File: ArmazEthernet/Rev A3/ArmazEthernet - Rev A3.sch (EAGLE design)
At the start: 109 parts, among them J1 22-05-7028-02, P1 RB1-125BAG1A, T1 H1102FNL, T2 H1102FNL, U3 KSZ8995MA, U4 AT24C02C-SSHM-B, X1 NE8FAV, X2 NE8FAV, Y1 8Z-25.000MHZMAAJ-T

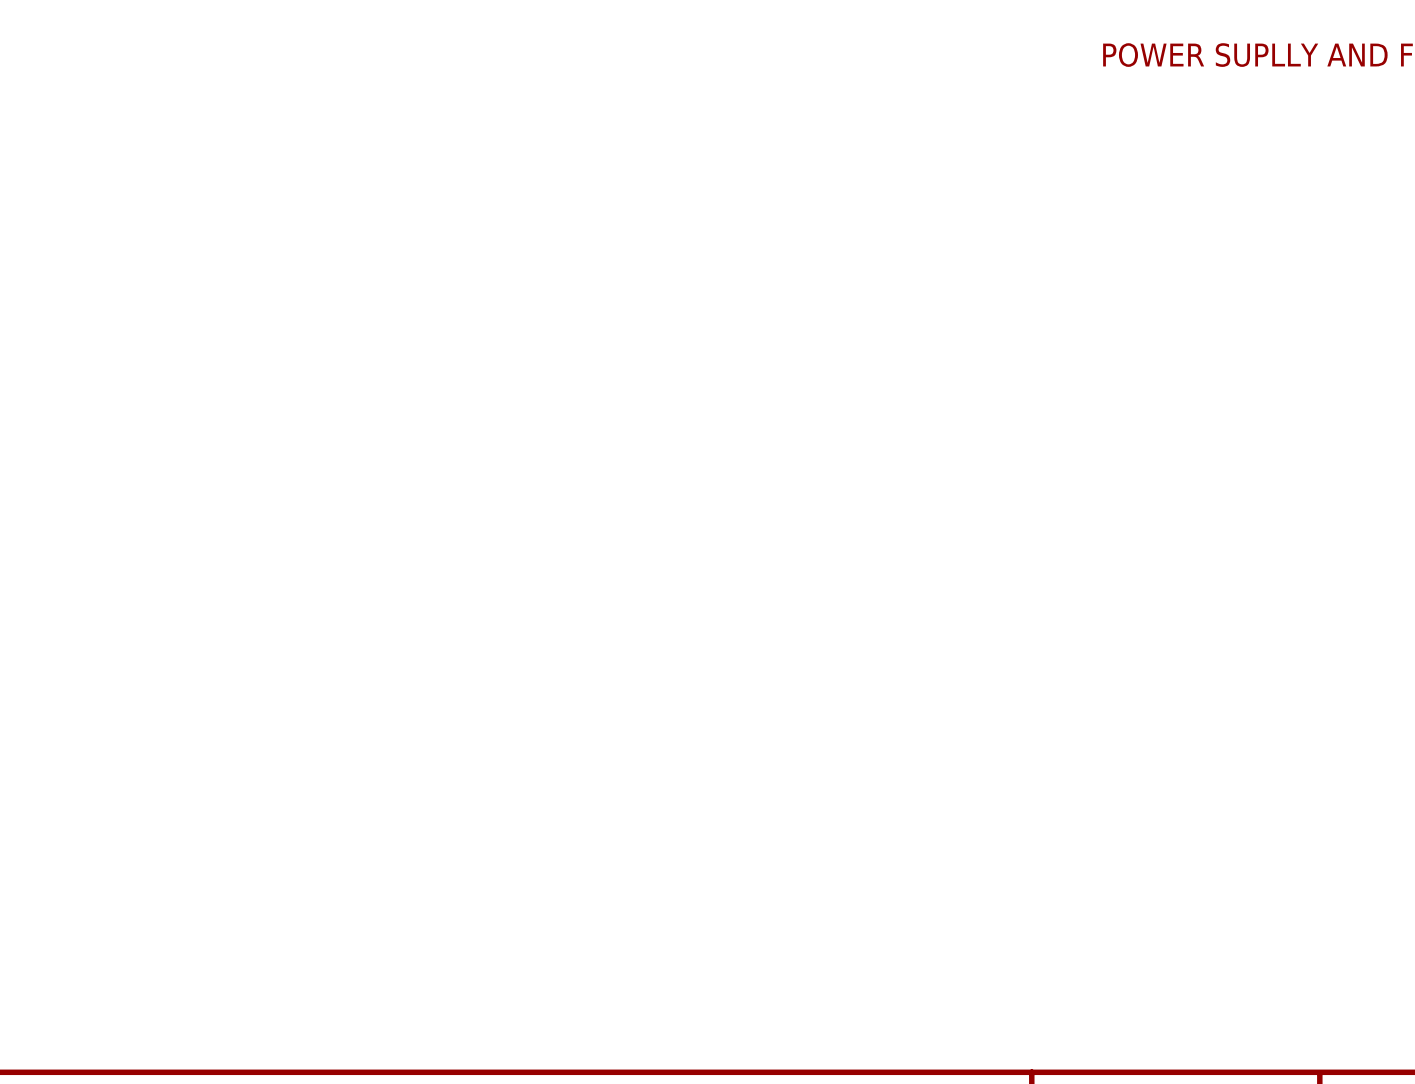
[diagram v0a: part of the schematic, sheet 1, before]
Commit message: Change the 3V3 and 1V8 circuit and place the component
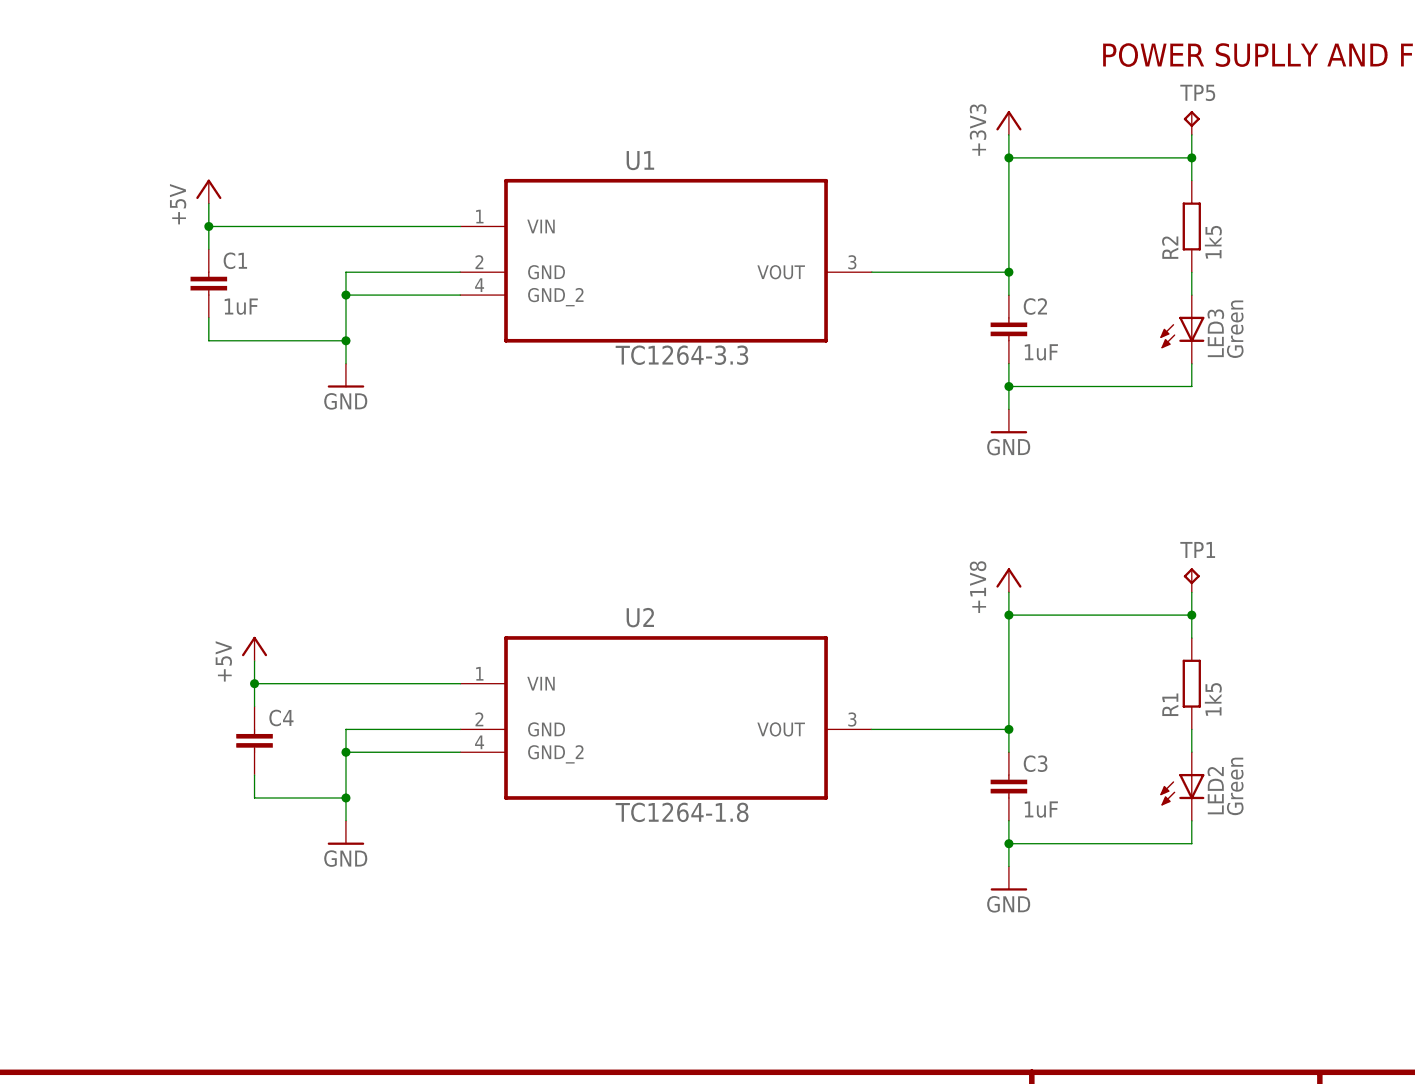
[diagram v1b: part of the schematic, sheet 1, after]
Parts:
- added C1, C2, C3: 1uF, rcl:C-EUC0603
- added C4: (no value), rcl:C-EUC0603
- added LED2, LED3: Green, led:LEDCHIP-LED0603
- added R1, R2: 1k5, rcl:R-EU_R0603
- added TP1, TP5: TPB1,27, testpad:TPB1,27
- added U1: TC1264-3.3, microchip-6:TC1264-3.3
- added U2: TC1264-1.8, microchip-6:TC1264-1.8
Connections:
- new net N$2: LED2.A, R1.1
- new net N$6: LED3.A, R2.1
- net +1V8: now also C3.1, R1.2, TP1.TP, U2.VOUT
- net +3V3: now also C2.1, R2.2, TP5.TP, U1.VOUT
- net +5V: now also C1.1, C4.1, U1.VIN, U2.VIN
- net GND: now also C1.2, C2.2, C3.2, C4.2, LED2.C, LED3.C, U1.GND, U1.GND_2, U2.GND, U2.GND_2

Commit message: switch the ethernet port on micrel component to improve the route : eth1 -> 3, eth2 -> 1 and eth 3-> 2
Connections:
- net L1-1: now also U3B.LED3-0; no longer U3B.LED1-0
- net L1-2: now also U3B.LED3-1; no longer U3B.LED1-1
- net L2-1: now also U3B.LED1-0; no longer U3B.LED2-0
- net L2-2: now also U3B.LED1-1; no longer U3B.LED2-1
- net L3-1: now also U3B.LED2-0; no longer U3B.LED3-0
- net L3-2: now also U3B.LED2-1; no longer U3B.LED3-1
- net RX1_ISO_N: now also U3A.RXM3; no longer U3A.RXM1
- net RX1_ISO_P: now also U3A.RXP3; no longer U3A.RXP1
- net RX2_ISO_N: now also U3A.RXM1; no longer U3A.RXM2
- net RX2_ISO_P: now also U3A.RXP1; no longer U3A.RXP2
- net RX3_ISO_N: now also U3A.RXM2; no longer U3A.RXM3
- net RX3_ISO_P: now also U3A.RXP2; no longer U3A.RXP3
- net TX1_ISO_N: now also U3A.TXM3; no longer U3A.TXM1
- net TX1_ISO_P: now also U3A.TXP3; no longer U3A.TXP1
- net TX2_ISO_N: now also U3A.TXM1; no longer U3A.TXM2
- net TX2_ISO_P: now also U3A.TXP1; no longer U3A.TXP2
- net TX3_ISO_N: now also U3A.TXM2; no longer U3A.TXM3
- net TX3_ISO_P: now also U3A.TXP2; no longer U3A.TXP3
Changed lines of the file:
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@@
 <net name="RX3_ISO_P" class="0">
 <segment>
-<wire x1="157.48" y1="205.74" x2="149.86" y2="205.74" width="0.1524" layer="91"/>
-<label x="149.86" y="205.74" size="1.27" layer="95" rot="R180" xref="yes"/>
-<pinref part="U3" gate="A" pin="RXP3"/>
+<wire x1="157.48" y1="220.98" x2="147.32" y2="220.98" width="0.1524" layer="91"/>
+<label x="147.32" y="220.98" size="1.27" layer="95" rot="R180" xref="yes"/>
+<pinref part="U3" gate="A" pin="RXP2"/>
 </segment>
 </net>
 <net name="RX3_ISO_N" class="0">
 <segment>
-<wire x1="157.48" y1="203.2" x2="149.86" y2="203.2" width="0.1524" layer="91"/>
-<label x="149.86" y="203.2" size="1.27" layer="95" rot="R180" xref="yes"/>
-<pinref part="U3" gate="A" pin="RXM3"/>
+<wire x1="157.48" y1="218.44" x2="147.32" y2="218.44" width="0.1524" layer="91"/>
+<label x="147.32" y="218.44" size="1.27" layer="95" rot="R180" xref="yes"/>
+<pinref part="U3" gate="A" pin="RXM2"/>
 </segment>
 </net>
 <net name="TX3_ISO_N" class="0">
 <segment>
-<wire x1="238.76" y1="172.72" x2="246.38" y2="172.72" width="0.1524" layer="91"/>
-<label x="246.38" y="172.72" size="1.27" layer="95" xref="yes"/>
-<pinref part="U3" gate="A" pin="TXM3"/>
+<wire x1="238.76" y1="165.1" x2="246.38" y2="165.1" width="0.1524" layer="91"/>
+<label x="246.38" y="165.1" size="1.27" layer="95" xref="yes"/>
+<pinref part="U3" gate="A" pin="TXM2"/>
 </segment>
 </net>
 <net name="TX3_ISO_P" class="0">
 <segment>
-<wire x1="238.76" y1="170.18" x2="246.38" y2="170.18" width="0.1524" layer="91"/>
-<label x="246.38" y="170.18" size="1.27" layer="95" xref="yes"/>
-<pinref part="U3" gate="A" pin="TXP3"/>
+<wire x1="238.76" y1="162.56" x2="246.38" y2="162.56" width="0.1524" layer="91"/>
+<label x="246.38" y="162.56" size="1.27" layer="95" xref="yes"/>
+<pinref part="U3" gate="A" pin="TXP2"/>
 </segment>
 </net>
@@
 <net name="L3-1" class="0">
 <segment>
-<pinref part="U3" gate="B" pin="LED3-0"/>
-<wire x1="241.3" y1="78.74" x2="251.46" y2="78.74" width="0.1524" layer="91"/>
-<label x="251.46" y="78.74" size="1.27" layer="95" xref="yes"/>
+<wire x1="241.3" y1="91.44" x2="251.46" y2="91.44" width="0.1524" layer="91"/>
+<label x="251.46" y="91.44" size="1.27" layer="95" xref="yes"/>
+<pinref part="U3" gate="B" pin="LED2-0"/>
 </segment>
 </net>
 <net name="L3-2" class="0">
 <segment>
-<pinref part="U3" gate="B" pin="LED3-1"/>
-<wire x1="241.3" y1="76.2" x2="251.46" y2="76.2" width="0.1524" layer="91"/>
-<label x="251.46" y="76.2" size="1.27" layer="95" xref="yes"/>
+<wire x1="241.3" y1="88.9" x2="251.46" y2="88.9" width="0.1524" layer="91"/>
+<label x="251.46" y="88.9" size="1.27" layer="95" xref="yes"/>
+<pinref part="U3" gate="B" pin="LED2-1"/>
 </segment>
 </net>
@@
 <net name="L1-1" class="0">
 <segment>
-<pinref part="U3" gate="B" pin="LED1-0"/>
+<wire x1="241.3" y1="78.74" x2="251.46" y2="78.74" width="0.1524" layer="91"/>
+<label x="251.46" y="78.74" size="1.27" layer="95" xref="yes"/>
+<pinref part="U3" gate="B" pin="LED3-0"/>
+</segment>
+</net>
+<net name="L1-2" class="0">
+<segment>
+<wire x1="241.3" y1="76.2" x2="251.46" y2="76.2" width="0.1524" layer="91"/>
+<label x="251.46" y="76.2" size="1.27" layer="95" xref="yes"/>
+<pinref part="U3" gate="B" pin="LED3-1"/>
+</segment>
+</net>
+<net name="L2-1" class="0">
+<segment>
 <wire x1="241.3" y1="99.06" x2="251.46" y2="99.06" width="0.1524" layer="91"/>
 <label x="251.46" y="99.06" size="1.27" layer="95" xref="yes"/>
-</segment>
-</net>
-<net name="L1-2" class="0">
-<segment>
-<pinref part="U3" gate="B" pin="LED1-1"/>
+<pinref part="U3" gate="B" pin="LED1-0"/>
+</segment>
+</net>
+<net name="L2-2" class="0">
+<segment>
 <wire x1="241.3" y1="96.52" x2="251.46" y2="96.52" width="0.1524" layer="91"/>
 <label x="251.46" y="96.52" size="1.27" layer="95" xref="yes"/>
-</segment>
-</net>
-<net name="L2-1" class="0">
-<segment>
-<pinref part="U3" gate="B" pin="LED2-0"/>
-<wire x1="241.3" y1="91.44" x2="251.46" y2="91.44" width="0.1524" layer="91"/>
-<label x="251.46" y="91.44" size="1.27" layer="95" xref="yes"/>
-</segment>
-</net>
-<net name="L2-2" class="0">
-<segment>
-<pinref part="U3" gate="B" pin="LED2-1"/>
-<wire x1="241.3" y1="88.9" x2="251.46" y2="88.9" width="0.1524" layer="91"/>
-<label x="251.46" y="88.9" size="1.27" layer="95" xref="yes"/>
+<pinref part="U3" gate="B" pin="LED1-1"/>
 </segment>
 </net>
 <net name="RX1_ISO_P" class="0">
 <segment>
+<wire x1="157.48" y1="205.74" x2="147.32" y2="205.74" width="0.1524" layer="91"/>
+<label x="147.32" y="205.74" size="1.27" layer="95" rot="R180" xref="yes"/>
+<pinref part="U3" gate="A" pin="RXP3"/>
+</segment>
+</net>
+<net name="RX1_ISO_N" class="0">
+<segment>
+<wire x1="157.48" y1="203.2" x2="147.32" y2="203.2" width="0.1524" layer="91"/>
+<label x="147.32" y="203.2" size="1.27" layer="95" rot="R180" xref="yes"/>
+<pinref part="U3" gate="A" pin="RXM3"/>
+</segment>
+</net>
+<net name="RX2_ISO_P" class="0">
+<segment>
+<wire x1="157.48" y1="231.14" x2="147.32" y2="231.14" width="0.1524" layer="91"/>
+<label x="147.32" y="231.14" size="1.27" layer="95" rot="R180" xref="yes"/>
 <pinref part="U3" gate="A" pin="RXP1"/>
-<wire x1="157.48" y1="231.14" x2="149.86" y2="231.14" width="0.1524" layer="91"/>
-<label x="149.86" y="231.14" size="1.27" layer="95" rot="R180" xref="yes"/>
-</segment>
-</net>
-<net name="RX1_ISO_N" class="0">
-<segment>
+</segment>
+</net>
+<net name="RX2_ISO_N" class="0">
+<segment>
+<wire x1="157.48" y1="228.6" x2="147.32" y2="228.6" width="0.1524" layer="91"/>
+<label x="147.32" y="228.6" size="1.27" layer="95" rot="R180" xref="yes"/>
 <pinref part="U3" gate="A" pin="RXM1"/>
-<wire x1="157.48" y1="228.6" x2="149.86" y2="228.6" width="0.1524" layer="91"/>
-<label x="149.86" y="228.6" size="1.27" layer="95" rot="R180" xref="yes"/>
-</segment>
-</net>
-<net name="RX2_ISO_P" class="0">
-<segment>
-<pinref part="U3" gate="A" pin="RXP2"/>
-<wire x1="157.48" y1="220.98" x2="149.86" y2="220.98" width="0.1524" layer="91"/>
-<label x="149.86" y="220.98" size="1.27" layer="95" rot="R180" xref="yes"/>
-</segment>
-</net>
-<net name="RX2_ISO_N" class="0">
-<segment>
-<wire x1="157.48" y1="218.44" x2="149.86" y2="218.44" width="0.1524" layer="91"/>
-<label x="149.86" y="218.44" size="1.27" layer="95" rot="R180" xref="yes"/>
-<pinref part="U3" gate="A" pin="RXM2"/>
 </segment>
 </net>
 <net name="TX2_ISO_N" class="0">
-<segment>
-<pinref part="U3" gate="A" pin="TXM2"/>
-<wire x1="238.76" y1="165.1" x2="246.38" y2="165.1" width="0.1524" layer="91"/>
-<label x="246.38" y="165.1" size="1.27" layer="95" xref="yes"/>
-</segment>
-</net>
-<net name="TX2_ISO_P" class="0">
-<segment>
-<wire x1="238.76" y1="162.56" x2="246.38" y2="162.56" width="0.1524" layer="91"/>
-<label x="246.38" y="162.56" size="1.27" layer="95" xref="yes"/>
-<pinref part="U3" gate="A" pin="TXP2"/>
-</segment>
-</net>
-<net name="TX1_ISO_N" class="0">
 <segment>
 <wire x1="238.76" y1="160.02" x2="246.38" y2="160.02" width="0.1524" layer="91"/>
@@
 </segment>
 </net>
-<net name="TX1_ISO_P" class="0">
+<net name="TX2_ISO_P" class="0">
 <segment>
 <wire x1="238.76" y1="157.48" x2="246.38" y2="157.48" width="0.1524" layer="91"/>
@@
 </segment>
 </net>
+<net name="TX1_ISO_N" class="0">
+<segment>
+<wire x1="238.76" y1="172.72" x2="246.38" y2="172.72" width="0.1524" layer="91"/>
+<label x="246.38" y="172.72" size="1.27" layer="95" xref="yes"/>
+<pinref part="U3" gate="A" pin="TXM3"/>
+</segment>
+</net>
+<net name="TX1_ISO_P" class="0">
+<segment>
+<wire x1="238.76" y1="170.18" x2="246.38" y2="170.18" width="0.1524" layer="91"/>
+<label x="246.38" y="170.18" size="1.27" layer="95" xref="yes"/>
+<pinref part="U3" gate="A" pin="TXP3"/>
+</segment>
+</net>
